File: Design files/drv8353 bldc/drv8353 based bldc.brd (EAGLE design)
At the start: 127 x 127 mm, 118 parts, among them IC1 DRV8353RSRGZT, J3 2X6 FEMALE, J4 B06B-HCMKK

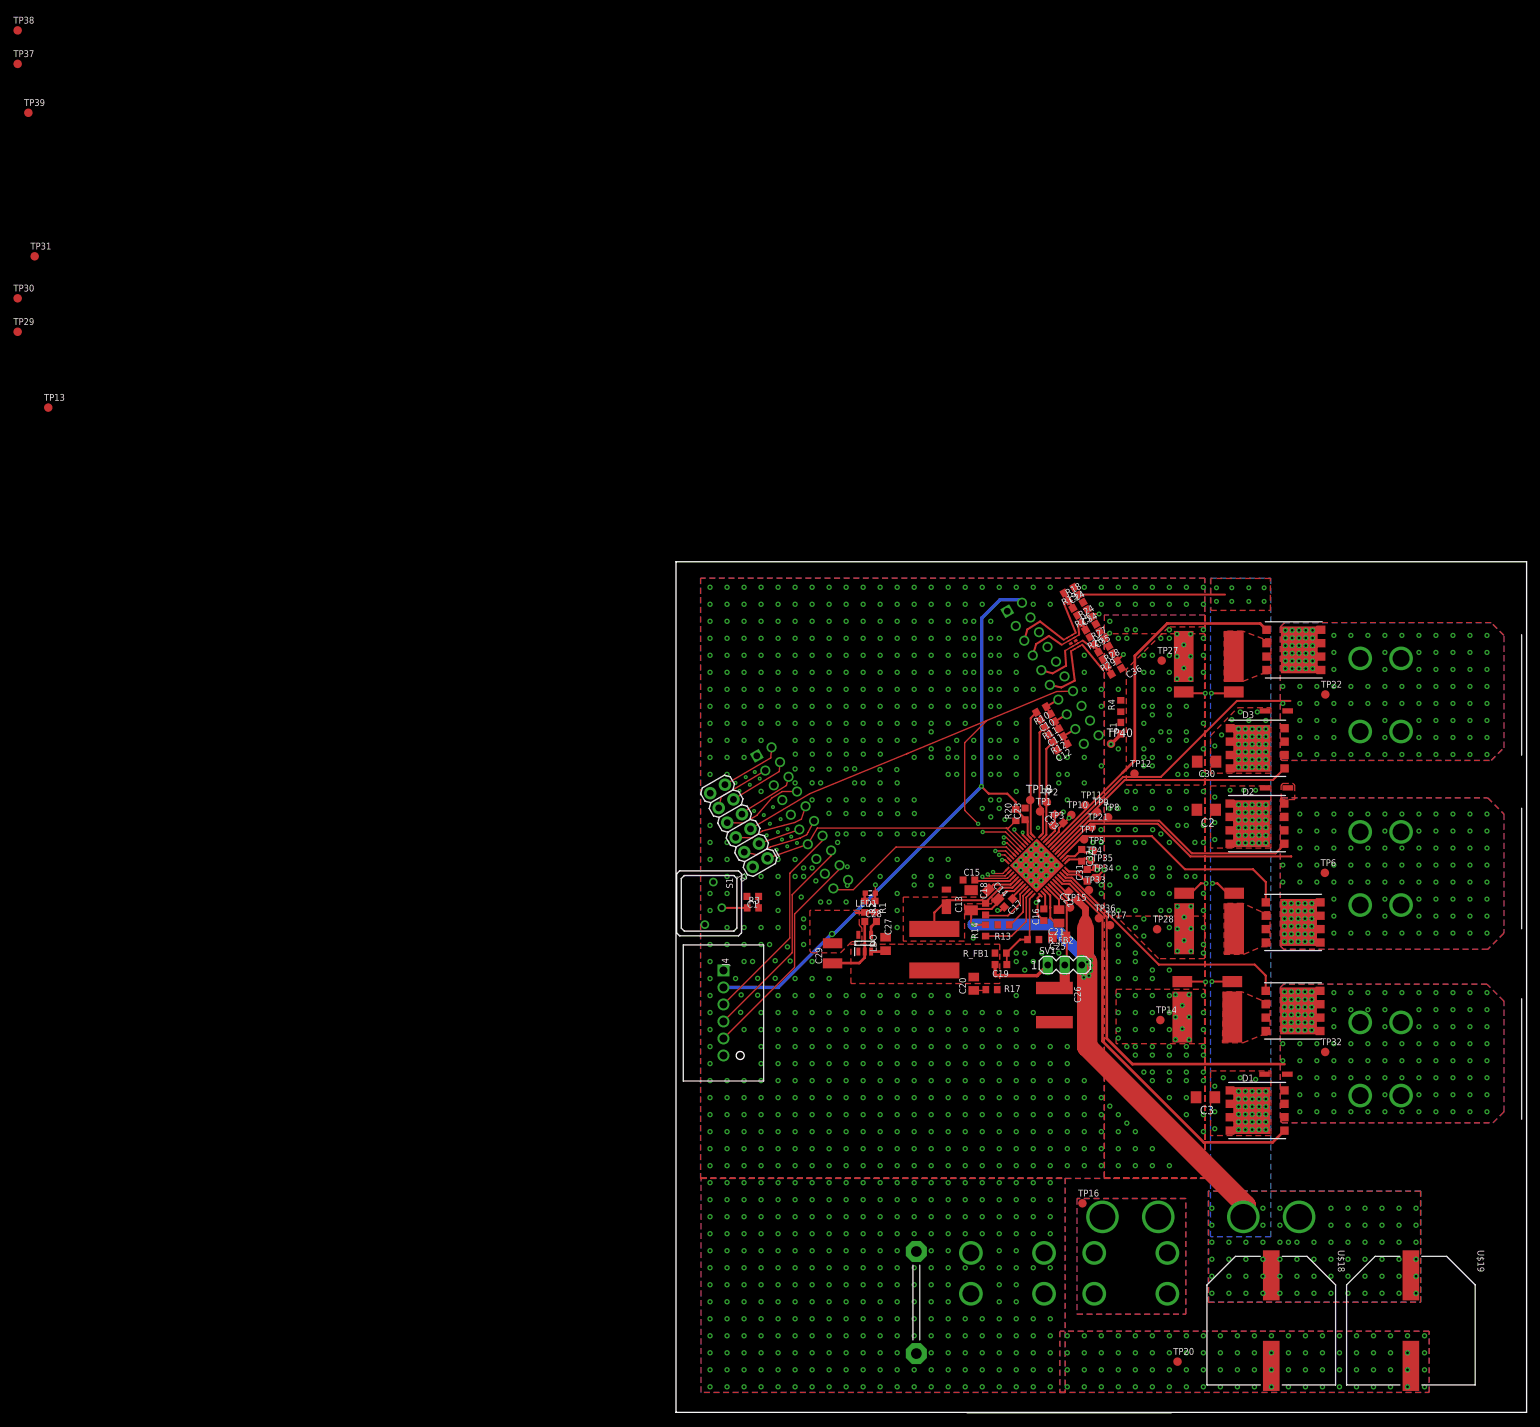
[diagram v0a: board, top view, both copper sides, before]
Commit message: fixes: c31-33 closer to fets, spacing of ABCPhases, layout of drv internal buck regulator
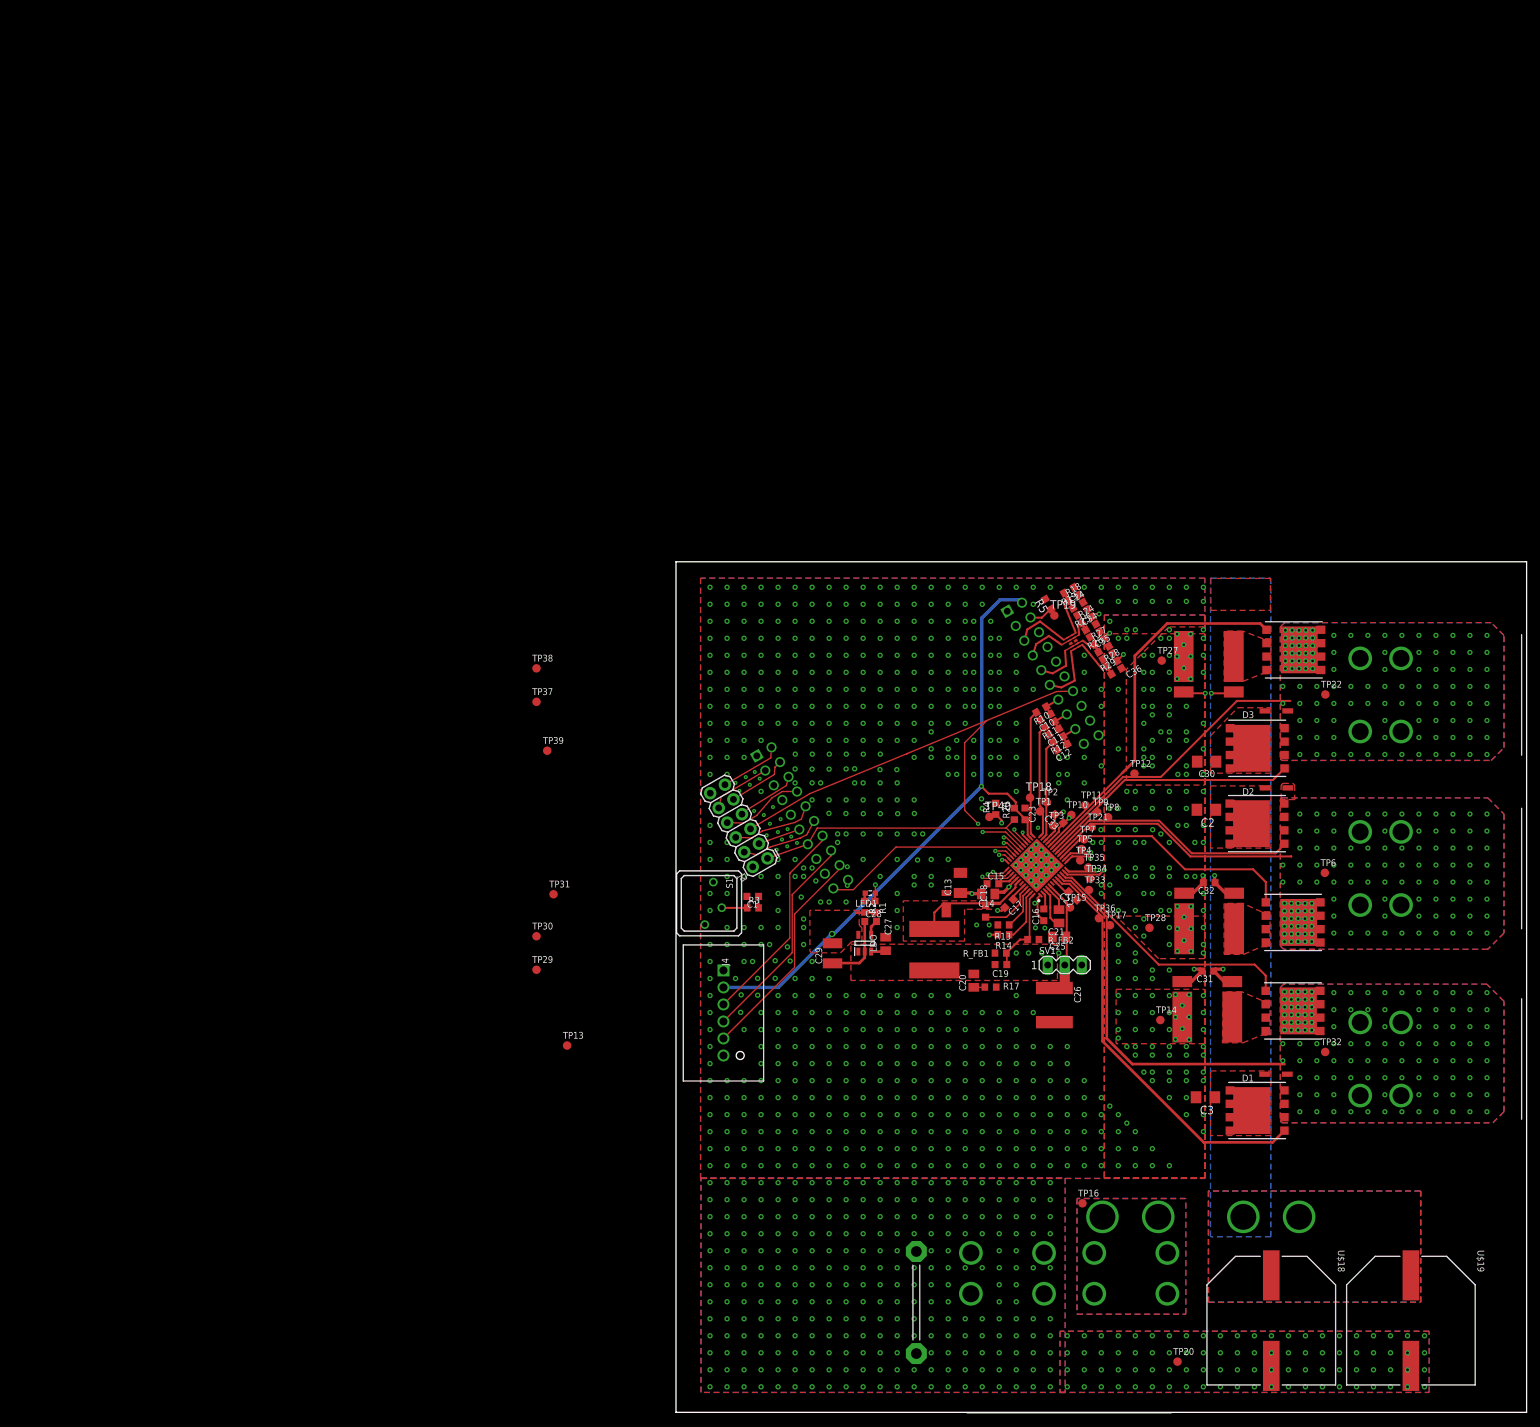
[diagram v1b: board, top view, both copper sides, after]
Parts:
- removed L1: 33nH/±5%/500mA, SparkFun-Coils:0603
- added R5: 0, resistor:R0603
- added TP19: TPB1,27, testpad:B1,27
- moved TP29 122.8 mm to (-20.8, 66.1)
- moved TP30 122.8 mm to (-20.8, 71.1)
- moved TP37 122.8 mm to (-20.8, 106.1)
- moved TP38 122.8 mm to (-20.8, 111.1)
- moved TP31 122.8 mm to (-18.3, 77.4)
- moved TP39 122.8 mm to (-19.2, 98.8)
- moved TP13 122.8 mm to (-16.3, 54.8)
- moved R4 24.2 mm to (47.7, 90.1)
- moved C31 23.0 mm to (79.4, 65.9), turned to 180 degrees
- moved TP40 21.2 mm to (46.8, 88.9)
- moved C32 19.5 mm to (79.6, 79.1), turned to 180 degrees
- moved C15 3.62 mm to (47.3, 78.9)
- moved C13 3.05 mm to (42.5, 79.0)
- moved R14 2.74 mm to (48.9, 71.3), turned to 0 degrees
- moved TP5 1.74 mm to (60.5, 84.1)
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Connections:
- removed net N$21: L1.2, R4.1
- new net PGND: R5.1, TP19.TP, U$2.2
- net AGND: now also R4.1; no longer L1.1, U$2.2
- net GND: now also R5.2
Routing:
- net VDRAIN: track 119.0 -> 51.9 mm, vias 195 -> 2
- net AGND: track 49.1 -> 8.40 mm, vias 3 -> 2
- net CPHASE: track 103.5 -> 73.0 mm
- net VBUCK: track 12.4 -> 2.22 mm
- net PGND: track 0.00 -> 4.99 mm
- net RT/SD: track 11.5 -> 7.97 mm
- net N$1: track 6.27 -> 2.79 mm
- net SNA: track 34.8 -> 32.9 mm
- net APHASE: track 175.4 -> 177.2 mm
- net SPA: track 36.3 -> 37.9 mm
- net SPB: track 29.3 -> 30.0 mm
- net GND: track 11.2 -> 10.5 mm, vias 1188 -> 1185

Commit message: some small changes
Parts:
- moved C19 5.43 mm to (53.0, 69.9), turned to 90 degrees
- moved R_FB1 3.38 mm to (51.6, 69.9), turned to 270 degrees
- moved L3 2.13 mm to (40.7, 69.2)
- moved C20 2.01 mm to (46.5, 64.4)
- moved R17 2.01 mm to (49.0, 63.4)
- moved D4 1.37 mm to (39.0, 76.1)
- moved R_FB2 1.32 mm to (54.5, 69.9), turned to 90 degrees
- moved C15 0.28 mm to (47.6, 78.9)
- moved C14 0.08 mm to (46.6, 77.3)
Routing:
- net FB: track 12.7 -> 9.95 mm
- net GND: track 10.5 -> 12.4 mm, vias 1185 -> 1186
- net SW: track 17.6 -> 16.2 mm
- net VDRAIN: track 51.9 -> 53.1 mm, vias 2 -> 3

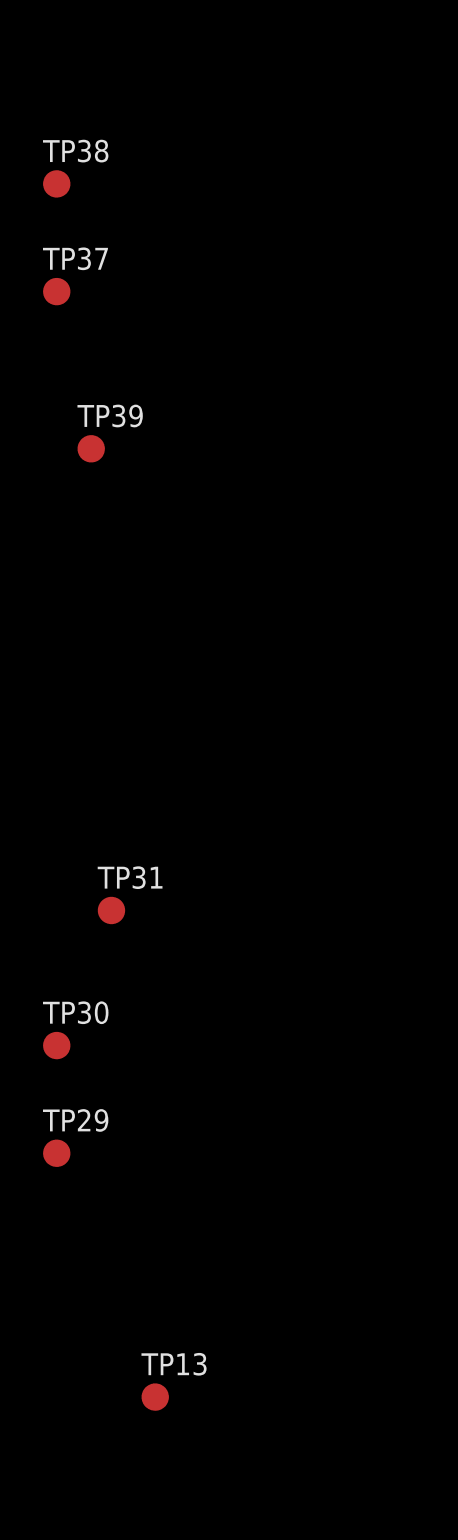
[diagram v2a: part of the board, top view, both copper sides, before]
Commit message: remoeved extraneous test points
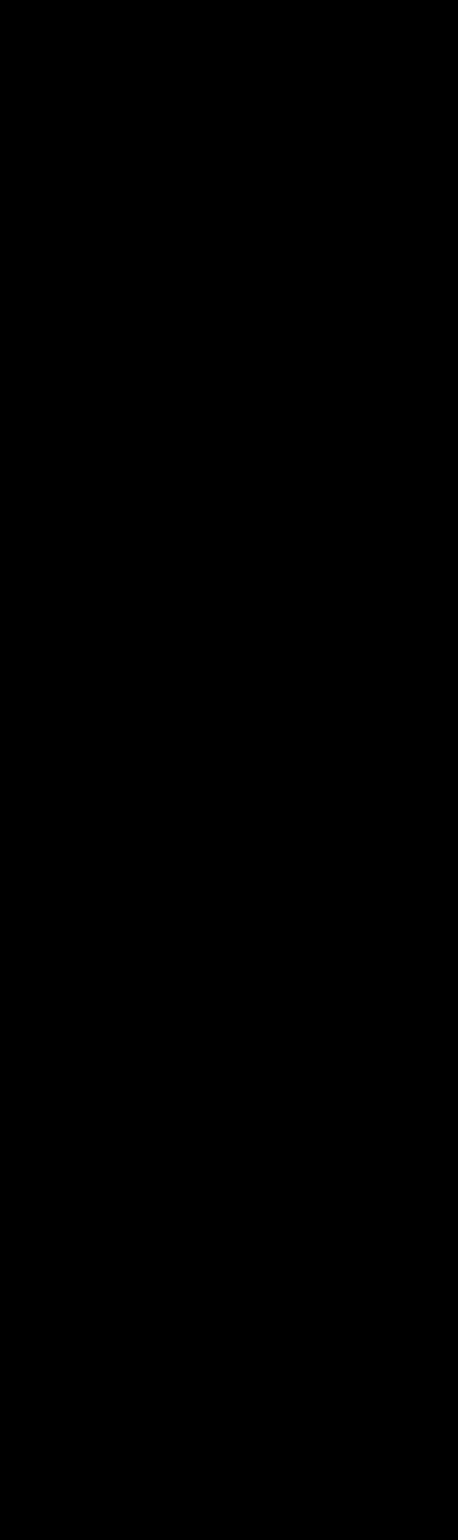
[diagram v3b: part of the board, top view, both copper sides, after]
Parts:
- removed TP13, TP29, TP30, TP31, TP37, TP38, TP39: TPB1,27, testpad:B1,27
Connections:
- removed net N$17: TP39.TP, U$2.8
- removed net N$18: TP38.TP, U$2.6
- removed net N$19: TP37.TP, U$2.5
- net ISENA: no longer TP29.TP
- net ISENB: no longer TP30.TP
- net ISENC: no longer TP31.TP
- net VCP: no longer TP13.TP
